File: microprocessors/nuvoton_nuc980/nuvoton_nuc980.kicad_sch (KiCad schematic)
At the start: 8 parts, among them SW3 SW_Push_Dual, U1 NUC980DK63YC

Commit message: feat: cotti leds with new library format
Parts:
- removed SW3: SW_Push_Dual, symbol Switch:SW_Push_Dual
- added SW3: SW_Push_Dual, Button_Switch_THT:SW_PUSH_6mm_H5mm, symbol cotti_switch:SW_Push_Dual
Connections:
- net EINT3: now also SW3.1, SW3.3
- net GND: now also SW3.2, SW3.4
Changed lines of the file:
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@@
-	)
-	(symbol
-		(lib_id "Switch:SW_Push_Dual")
-		(at 48.26 156.21 0)
-		(unit 1)
-		(exclude_from_sim no)
-		(in_bom yes)
-		(on_board yes)
-		(dnp no)
-		(fields_autoplaced yes)
-		(property "Reference" "SW3"
-			(at 48.26 146.05 0)
-			(effects
-				(font
-					(size 1.27 1.27)
-				)
-			)
-		)
-		(property "Value" "SW_Push_Dual"
-			(at 48.26 148.59 0)
-			(effects
-				(font
-					(size 1.27 1.27)
-				)
-			)
-		)
-		(property "Footprint" ""
-			(at 48.26 148.59 0)
-			(effects
-				(font
-					(size 1.27 1.27)
-				)
-				(hide yes)
-			)
-		)
-		(property "Datasheet" "~"
-			(at 48.26 156.21 0)
-			(effects
-				(font
-					(size 1.27 1.27)
-				)
-				(hide yes)
-			)
-		)
-		(property "Description" "Push button switch, generic, symbol, four pins"
-			(at 48.26 156.21 0)
-			(effects
-				(font
-					(size 1.27 1.27)
-				)
-				(hide yes)
-			)
-		)
-		(pin "1"
-		)
-		(pin "4"
-		)
-		(pin "2"
-		)
-		(pin "3"
-		)
-		(instances
-			(project ""
-				(path "/109442c7-6d61-4448-a955-a6cd87e17c77"
-					(reference "SW3")
-					(unit 1)
-				)
-			)
-		)
 	)
 	(symbol
@@
 					(unit 1)
 				)
+			)
+		)
+	)
+	(symbol
+		(lib_id "cotti_switch:SW_Push_Dual")
+		(at 48.26 156.21 0)
+		(unit 1)
+		(exclude_from_sim no)
+		(in_bom yes)
+		(on_board yes)
+		(dnp no)
+		(fields_autoplaced yes)
+		(property "Reference" "SW3"
+			(at 48.26 146.05 0)
+			(effects
+				(font
+					(size 1.27 1.27)
+				)
+			)
+		)
+		(property "Value" "SW_Push_Dual"
+			(at 48.26 148.59 0)
+			(effects
+				(font
+					(size 1.27 1.27)
+				)
+			)
+		)
+		(property "Footprint" "Button_Switch_THT:SW_PUSH_6mm_H5mm"
+			(at 46.482 123.952 0)
+			(effects
+				(font
+					(size 1.27 1.27)
+				)
+				(hide yes)
+			)
+		)
+		(property "Datasheet" "https://www.sameskydevices.com/product/resource/ts02.pdf"
+			(at 46.736 139.192 0)
+			(effects
+				(font
+					(size 1.27 1.27)
+				)
+				(hide yes)
+			)
+		)
+		(property "Description" "Tactile Switch SPST-NO Top Actuated Through Hole"
+			(at 47.498 143.51 0)
+			(effects
+				(font
+					(size 1.27 1.27)
+				)
+				(hide yes)
+			)
+		)
+		(property "Digikey" "https://www.digikey.com/en/products/detail/same-sky-formerly-cui-devices/TS02-66-60-BK-260-SCR-D/15634288"
+			(at 50.8 135.128 0)
+			(effects
+				(font
+					(size 1.27 1.27)
+				)
+				(hide yes)
+			)
+		)
+		(property "Mfr." "Same Sky (Formerly CUI Devices)"
+			(at 48.768 128.524 0)
+			(effects
+				(font
+					(size 1.27 1.27)
+				)
+				(hide yes)
+			)
+		)
+		(property "Mfr. P/N" "TS02-66-60-BK-260-SCR-D"
+			(at 48.26 131.318 0)
+			(effects
+				(font
+					(size 1.27 1.27)
+				)
+				(hide yes)
+			)
+		)
+		(pin "4"
+		)
+		(pin "3"
+		)
+		(pin "1"
+		)
+		(pin "2"
+		)
+		(instances
+			(project ""
+				(path "/109442c7-6d61-4448-a955-a6cd87e17c77"
+					(reference "SW3")
+					(unit 1)
+				)

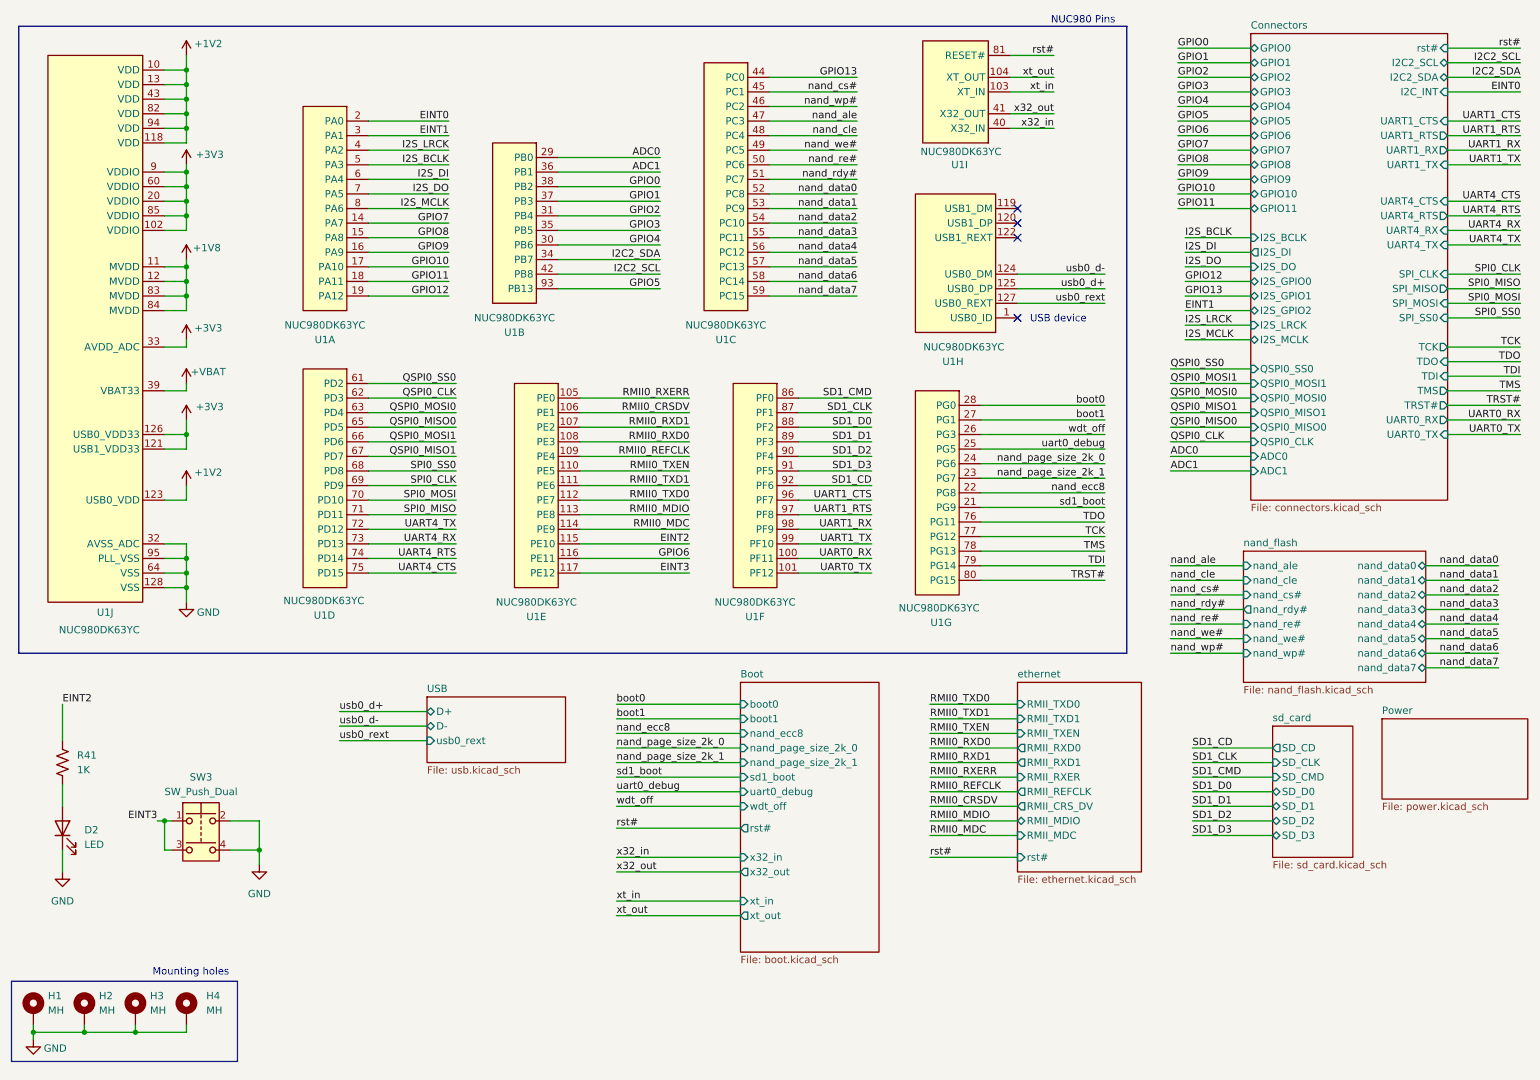
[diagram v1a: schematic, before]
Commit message: feat: ERC passing cotti-nuvoton
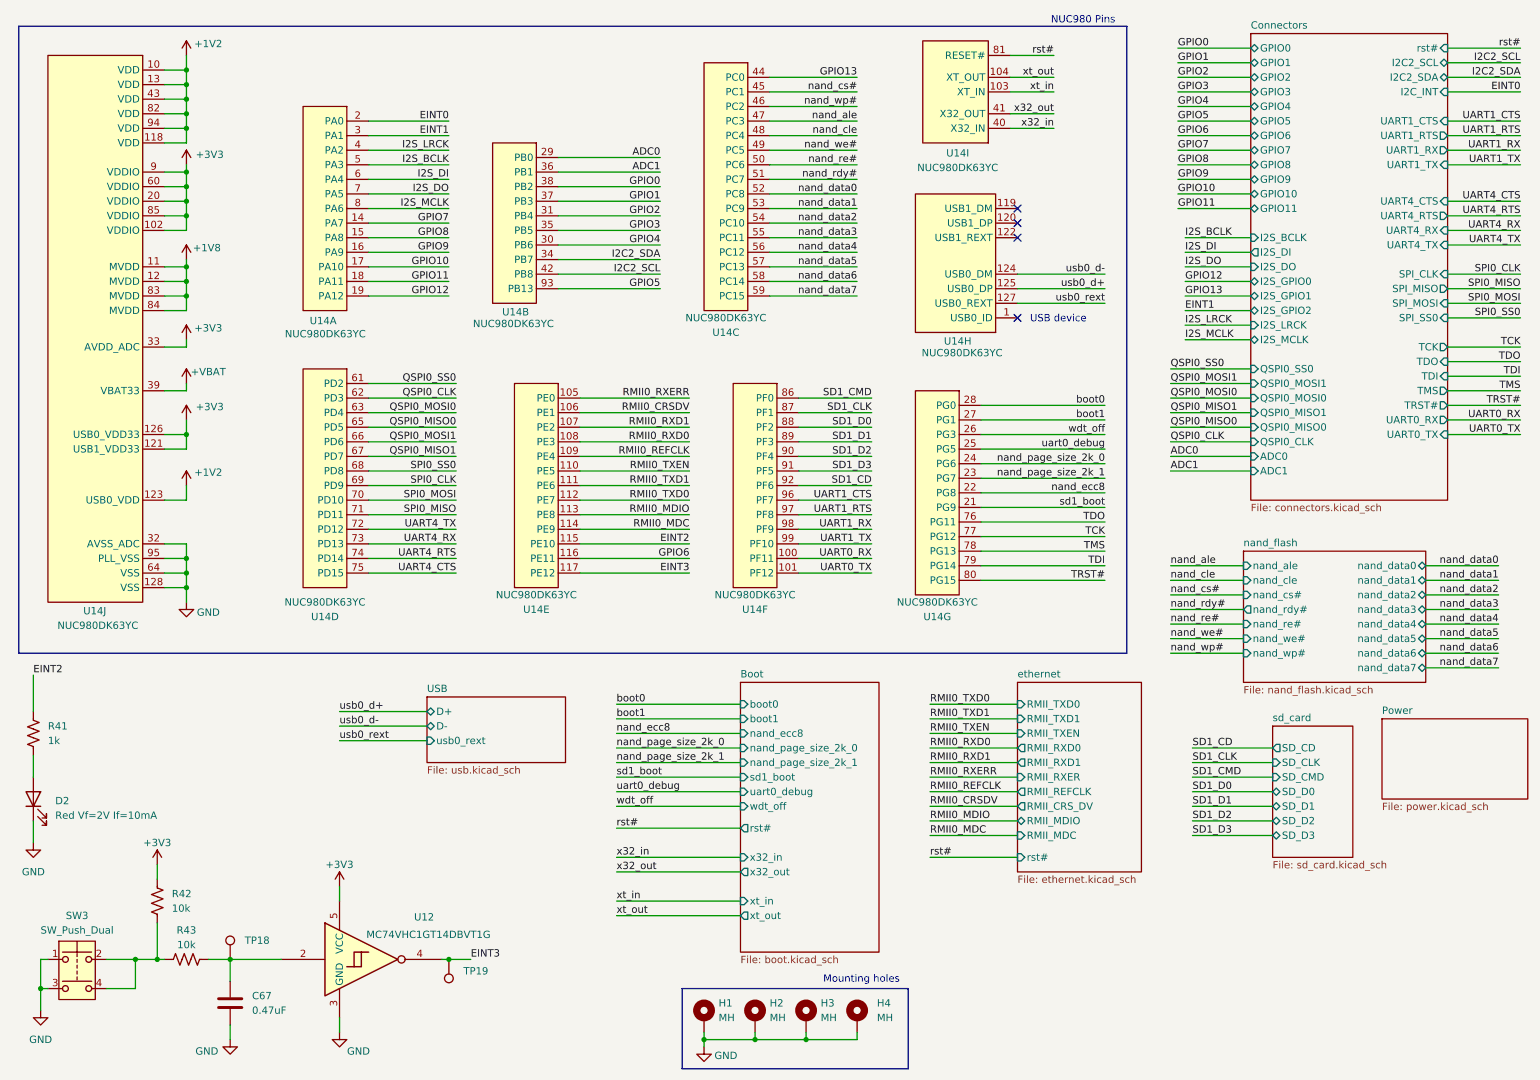
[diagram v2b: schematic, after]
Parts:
- removed D2: LED, symbol Device:LED
- removed U1: NUC980DK63YC, Package_QFP:LQFP-128_14x14mm_P0.4mm, symbol project_symbols:nuc980
- added C67: 0.47uF, Capacitor_SMD:C_0805_2012Metric_Pad1.18x1.45mm_HandSolder, symbol Device:C
- added D2: Red Vf=2V If=10mA, LED_SMD:LED_0603_1608Metric_Pad1.05x0.95mm_HandSolder, symbol cotti_leds:LED_Red_SMD
- added R42, R43: 10k, Resistor_SMD:R_0805_2012Metric_Pad1.20x1.40mm_HandSolder, symbol Device:R_US
- added TP18, TP19: TestPoint, TestPoint:TestPoint_Pad_D2.0mm, symbol Connector:TestPoint
- added U12: MC74VHC1GT14DBVT1G, Package_TO_SOT_SMD:SC-74A-5_1.55x2.9mm_P0.95mm, symbol cotti_ic:inverter_schmitt_input
- added U14: NUC980DK63YC, Package_QFP:LQFP-128_14x14mm_P0.4mm, symbol cotti_mcu:nuc980
- R41: value 1K -> 1k; footprint (none) -> Resistor_SMD:R_0805_2012Metric_Pad1.20x1.40mm_HandSolder; Digikey (none) -> https://www.digikey.com/en/products/detail/yageo/RC0805FR-1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; Mfr. (none) -> YAGEO; Mfr. P/N (none) -> RC0805FR-101KL
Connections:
- net +1V2: now also U14.10 (VDD), U14.118 (VDD), U14.123 (USB0_VDD), U14.13 (VDD), U14.43 (VDD), U14.82 (VDD), U14.94 (VDD)
- net +1V8: now also U14.11 (MVDD), U14.12 (MVDD), U14.83 (MVDD), U14.84 (MVDD)
- net +3V3: now also R42.1, U12.5 (VCC), U14.102 (VDDIO), U14.121 (USB1_VDD33), U14.126 (USB0_VDD33), U14.20 (VDDIO), U14.33 (AVDD_ADC), U14.60 (VDDIO), U14.85 (VDDIO), U14.9 (VDDIO)
- net +VBAT: now also U14.39 (VBAT33)
- net ADC0: now also U14.29 (PB0)
- net ADC1: now also U14.36 (PB1)
- net EINT0: now also U14.2 (PA0)
- net EINT1: now also U14.3 (PA1)
- net EINT2: now also U14.115 (PE10)
- net EINT3: now also TP19.1, U12.4, U14.117 (PE12); no longer SW3.1, SW3.3
- net GND: now also SW3.1, SW3.3, C67.2, D2.1 (K), U12.3 (GND), U14.128 (VSS), U14.32 (AVSS_ADC), U14.64 (VSS), U14.95 (PLL_VSS); no longer SW3.2, SW3.4
- net GPIO0: now also U14.38 (PB2)
- net GPIO1: now also U14.37 (PB3)
- net GPIO10: now also U14.17 (PA10)
- net GPIO11: now also U14.18 (PA11)
- net GPIO12: now also U14.19 (PA12)
- net GPIO13: now also U14.44 (PC0)
- net GPIO2: now also U14.31 (PB4)
- net GPIO3: now also U14.35 (PB5)
- net GPIO4: now also U14.30 (PB6)
- net GPIO5: now also U14.93 (PB13)
- net GPIO6: now also U14.116 (PE11)
- net GPIO7: now also U14.14 (PA7)
- net GPIO8: now also U14.15 (PA8)
- net GPIO9: now also U14.16 (PA9)
- net I2C2_SCL: now also U14.42 (PB8)
- net I2C2_SDA: now also U14.34 (PB7)
- net I2S_BCLK: now also U14.5 (PA3)
- net I2S_DI: now also U14.6 (PA4)
- net I2S_DO: now also U14.7 (PA5)
- net I2S_LRCK: now also U14.4 (PA2)
- net I2S_MCLK: now also U14.8 (PA6)
- net QSPI0_CLK: now also U14.62 (PD3)
- net QSPI0_MISO0: now also U14.65 (PD5)
- net QSPI0_MISO1: now also U14.67 (PD7)
- net QSPI0_MOSI0: now also U14.63 (PD4)
- net QSPI0_MOSI1: now also U14.66 (PD6)
- net QSPI0_SS0: now also U14.61 (PD2)
- net RMII0_CRSDV: now also U14.106 (PE1)
- net RMII0_MDC: now also U14.114 (PE9)
- net RMII0_MDIO: now also U14.113 (PE8)
- net RMII0_REFCLK: now also U14.109 (PE4)
- net RMII0_RXD0: now also U14.108 (PE3)
- net RMII0_RXD1: now also U14.107 (PE2)
- net RMII0_RXERR: now also U14.105 (PE0)
- net RMII0_TXD0: now also U14.112 (PE7)
- net RMII0_TXD1: now also U14.111 (PE6)
- net RMII0_TXEN: now also U14.110 (PE5)
- net SD1_CD: now also U14.92 (PF6)
- net SD1_CLK: now also U14.87 (PF1)
- net SD1_CMD: now also U14.86 (PF0)
- net SD1_D0: now also U14.88 (PF2)
- net SD1_D1: now also U14.89 (PF3)
- net SD1_D2: now also U14.90 (PF4)
- net SD1_D3: now also U14.91 (PF5)
- net SPI0_CLK: now also U14.69 (PD9)
- net SPI0_MISO: now also U14.71 (PD11)
- net SPI0_MOSI: now also U14.70 (PD10)
- net SPI0_SS0: now also U14.68 (PD8)
- net TCK: now also U14.77 (PG12)
- net TDI: now also U14.79 (PG14)
- net TDO: now also U14.76 (PG11)
- net TMS: now also U14.78 (PG13)
- net TRST#: now also U14.80 (PG15)
- net UART0_RX: now also U14.100 (PF11)
- net UART0_TX: now also U14.101 (PF12)
- net UART1_CTS: now also U14.96 (PF7)
- net UART1_RTS: now also U14.97 (PF8)
- net UART1_RX: now also U14.98 (PF9)
- net UART1_TX: now also U14.99 (PF10)
- net UART4_CTS: now also U14.75 (PD15)
- net UART4_RTS: now also U14.74 (PD14)
- net UART4_RX: now also U14.73 (PD13)
- net UART4_TX: now also U14.72 (PD12)
- net boot0: now also U14.28 (PG0)
- net boot1: now also U14.27 (PG1)
- net nand_ale: now also U14.47 (PC3)
- net nand_cle: now also U14.48 (PC4)
- net nand_cs#: now also U14.45 (PC1)
- net nand_data0: now also U14.52 (PC8)
- net nand_data1: now also U14.53 (PC9)
- net nand_data2: now also U14.54 (PC10)
- net nand_data3: now also U14.55 (PC11)
- net nand_data4: now also U14.56 (PC12)
- net nand_data5: now also U14.57 (PC13)
- net nand_data6: now also U14.58 (PC14)
- net nand_data7: now also U14.59 (PC15)
- net nand_ecc8: now also U14.22 (PG8)
- net nand_page_size_2k_0: now also U14.24 (PG6)
- net nand_page_size_2k_1: now also U14.23 (PG7)
- net nand_rdy#: now also U14.51 (PC7)
- net nand_re#: now also U14.50 (PC6)
- net nand_we#: now also U14.49 (PC5)
- net nand_wp#: now also U14.46 (PC2)
- net rst#: now also U14.81 (RESET#)
- net sd1_boot: now also U14.21 (PG9)
- net uart0_debug: now also U14.25 (PG5)
- net usb0_d+: now also U14.125 (USB0_DP)
- net usb0_d-: now also U14.124 (USB0_DM)
- net usb0_rext: now also U14.127 (USB0_REXT)
- net wdt_off: now also U14.26 (PG3)
- net x32_in: now also U14.40 (X32_IN)
- net x32_out: now also U14.41 (X32_OUT)
- net xt_in: now also U14.103 (XT_IN)
- net xt_out: now also U14.104 (XT_OUT)
- net at R41.2: now also D2.2 (A)
- new net: C67.1, R43.2, TP18.1, U12.2
- new net: R42.2, R43.1, SW3.2, SW3.4
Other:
- moved on the sheet: H1, H2, H3, H4, R41, SW3
